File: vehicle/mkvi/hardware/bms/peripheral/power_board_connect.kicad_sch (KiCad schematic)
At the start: 1 part

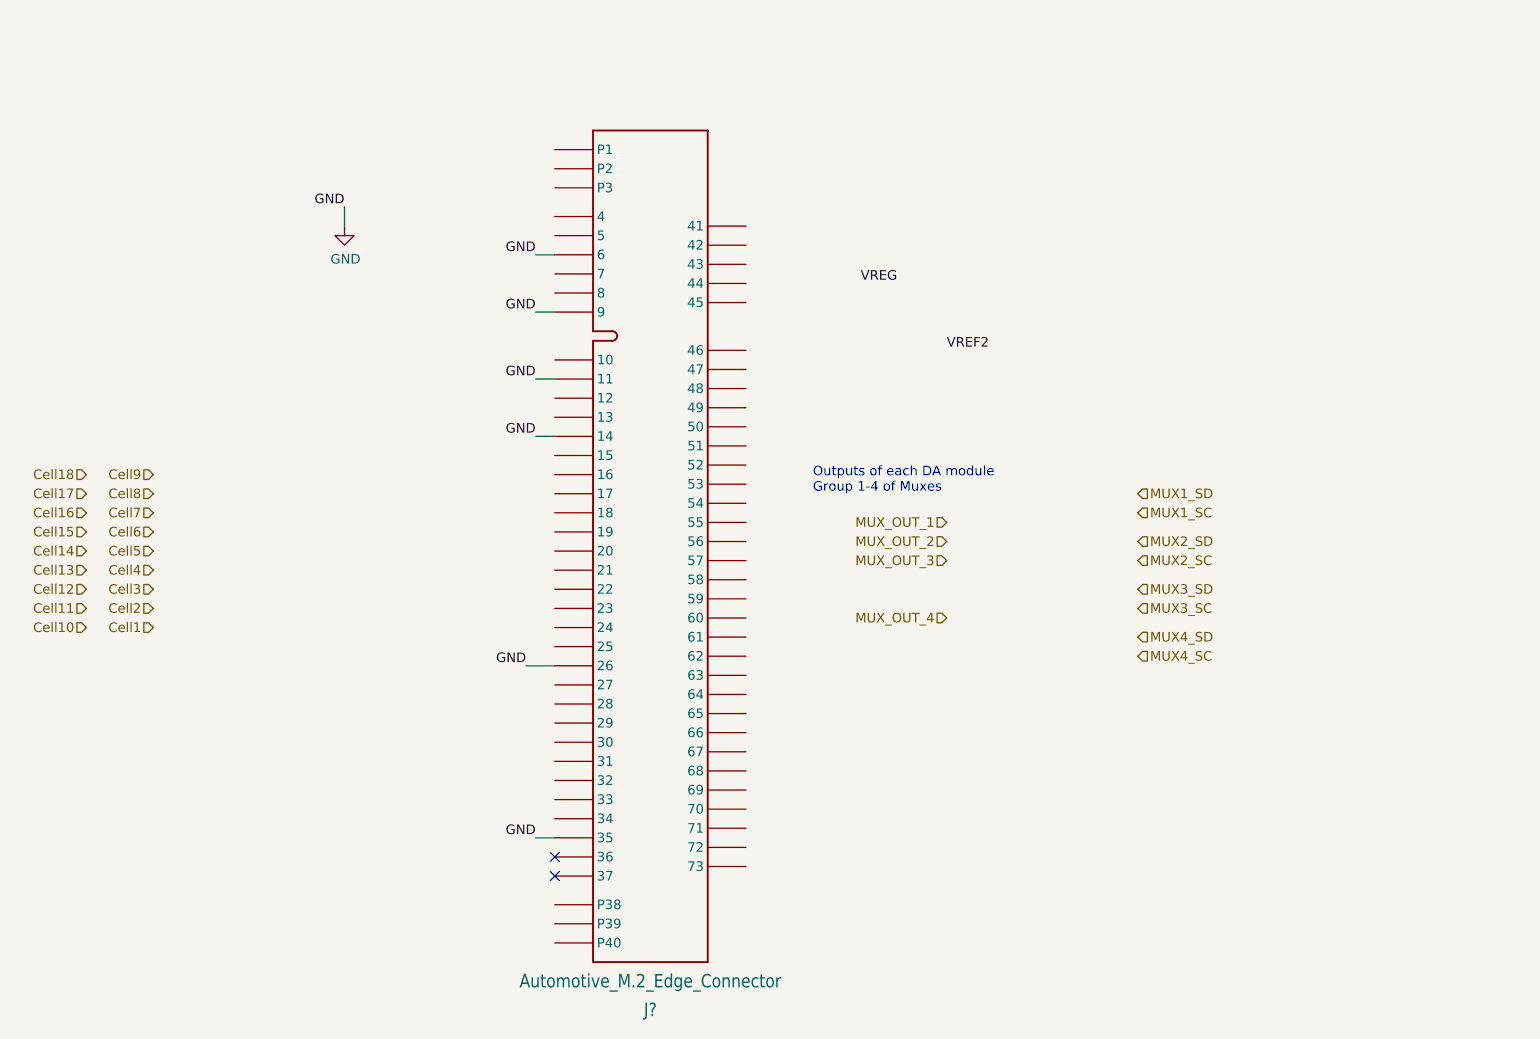
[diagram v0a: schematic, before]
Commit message: Fix transformer symbol and power flags
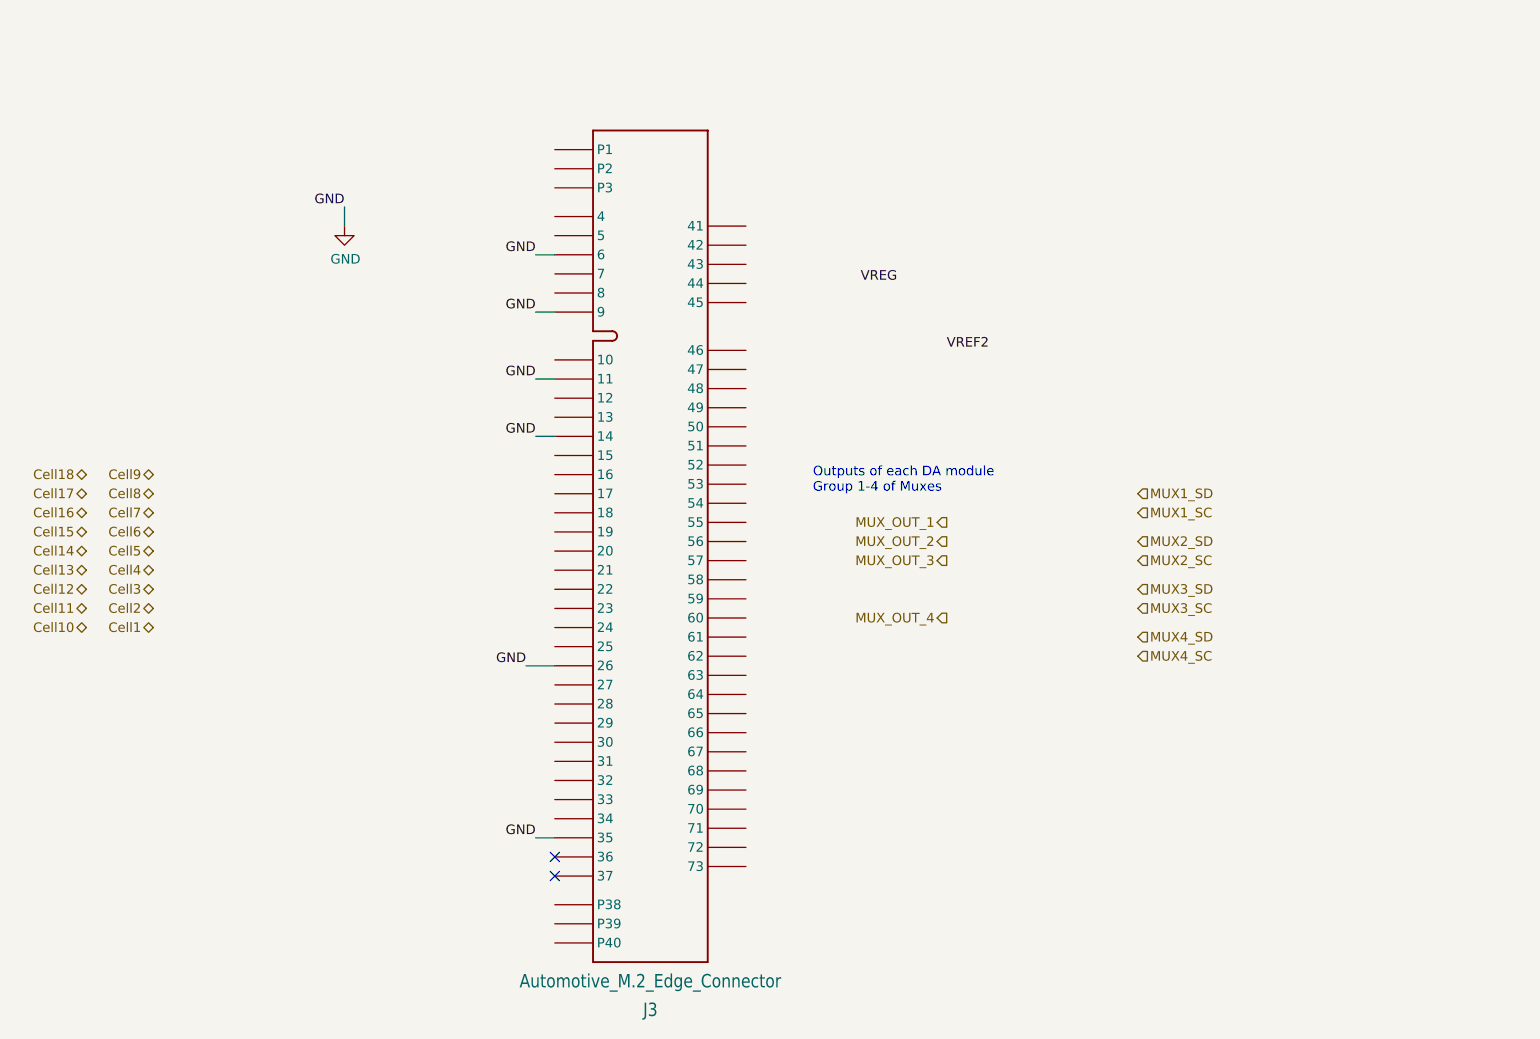
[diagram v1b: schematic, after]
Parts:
- gave numbers to parts that had none: 1
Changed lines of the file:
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@@
     (effects (font (size 1.27 1.27)) (justify right bottom))
   )
-  (hierarchical_label "MUX_OUT_4" (shape input) (at 180.34 102.87 180)
+  (hierarchical_label "MUX_OUT_4" (shape output) (at 180.34 102.87 180)
     (effects (font (size 1.27 1.27)) (justify right))
   )
-  (hierarchical_label "Cell13" (shape input) (at 66.04 96.52 180)
+  (hierarchical_label "Cell13" (shape bidirectional) (at 66.04 96.52 180)
     (effects (font (size 1.27 1.27)) (justify right))
   )
-  (hierarchical_label "Cell3" (shape input) (at 74.93 99.06 180)
+  (hierarchical_label "Cell3" (shape bidirectional) (at 74.93 99.06 180)
     (effects (font (size 1.27 1.27)) (justify right))
   )
-  (hierarchical_label "Cell1" (shape input) (at 74.93 104.14 180)
+  (hierarchical_label "Cell1" (shape bidirectional) (at 74.93 104.14 180)
     (effects (font (size 1.27 1.27)) (justify right))
   )
@@
     (effects (font (size 1.27 1.27)) (justify left))
   )
-  (hierarchical_label "Cell2" (shape input) (at 74.93 101.6 180)
+  (hierarchical_label "Cell2" (shape bidirectional) (at 74.93 101.6 180)
     (effects (font (size 1.27 1.27)) (justify right))
   )
-  (hierarchical_label "Cell12" (shape input) (at 66.04 99.06 180)
+  (hierarchical_label "Cell12" (shape bidirectional) (at 66.04 99.06 180)
     (effects (font (size 1.27 1.27)) (justify right))
   )
-  (hierarchical_label "Cell10" (shape input) (at 66.04 104.14 180)
+  (hierarchical_label "Cell10" (shape bidirectional) (at 66.04 104.14 180)
     (effects (font (size 1.27 1.27)) (justify right))
   )
@@
     (effects (font (size 1.27 1.27)) (justify left))
   )
-  (hierarchical_label "Cell11" (shape input) (at 66.04 101.6 180)
+  (hierarchical_label "Cell11" (shape bidirectional) (at 66.04 101.6 180)
     (effects (font (size 1.27 1.27)) (justify right))
   )
-  (hierarchical_label "Cell9" (shape input) (at 74.93 83.82 180)
+  (hierarchical_label "Cell9" (shape bidirectional) (at 74.93 83.82 180)
     (effects (font (size 1.27 1.27)) (justify right))
   )
-  (hierarchical_label "Cell18" (shape input) (at 66.04 83.82 180)
+  (hierarchical_label "Cell18" (shape bidirectional) (at 66.04 83.82 180)
     (effects (font (size 1.27 1.27)) (justify right))
   )
-  (hierarchical_label "MUX_OUT_3" (shape input) (at 180.34 95.25 180)
+  (hierarchical_label "MUX_OUT_3" (shape output) (at 180.34 95.25 180)
     (effects (font (size 1.27 1.27)) (justify right))
   )
-  (hierarchical_label "Cell17" (shape input) (at 66.04 86.36 180)
+  (hierarchical_label "Cell17" (shape bidirectional) (at 66.04 86.36 180)
     (effects (font (size 1.27 1.27)) (justify right))
   )
-  (hierarchical_label "MUX_OUT_2" (shape input) (at 180.34 92.71 180)
+  (hierarchical_label "MUX_OUT_2" (shape output) (at 180.34 92.71 180)
     (effects (font (size 1.27 1.27)) (justify right))
   )
-  (hierarchical_label "Cell5" (shape input) (at 74.93 93.98 180)
+  (hierarchical_label "Cell5" (shape bidirectional) (at 74.93 93.98 180)
     (effects (font (size 1.27 1.27)) (justify right))
   )
-  (hierarchical_label "Cell8" (shape input) (at 74.93 86.36 180)
+  (hierarchical_label "Cell8" (shape bidirectional) (at 74.93 86.36 180)
     (effects (font (size 1.27 1.27)) (justify right))
   )
@@
     (effects (font (size 1.27 1.27)) (justify left))
   )
-  (hierarchical_label "Cell6" (shape input) (at 74.93 91.44 180)
+  (hierarchical_label "Cell6" (shape bidirectional) (at 74.93 91.44 180)
     (effects (font (size 1.27 1.27)) (justify right))
   )
-  (hierarchical_label "MUX_OUT_1" (shape input) (at 180.34 90.17 180)
+  (hierarchical_label "MUX_OUT_1" (shape output) (at 180.34 90.17 180)
     (effects (font (size 1.27 1.27)) (justify right))
   )
@@
     (effects (font (size 1.27 1.27)) (justify left))
   )
-  (hierarchical_label "Cell16" (shape input) (at 66.04 88.9 180)
+  (hierarchical_label "Cell16" (shape bidirectional) (at 66.04 88.9 180)
     (effects (font (size 1.27 1.27)) (justify right))
   )
@@
     (effects (font (size 1.27 1.27)) (justify left))
   )
-  (hierarchical_label "Cell15" (shape input) (at 66.04 91.44 180)
+  (hierarchical_label "Cell15" (shape bidirectional) (at 66.04 91.44 180)
     (effects (font (size 1.27 1.27)) (justify right))
   )
-  (hierarchical_label "Cell4" (shape input) (at 74.93 96.52 180)
+  (hierarchical_label "Cell4" (shape bidirectional) (at 74.93 96.52 180)
     (effects (font (size 1.27 1.27)) (justify right))
   )
-  (hierarchical_label "Cell7" (shape input) (at 74.93 88.9 180)
+  (hierarchical_label "Cell7" (shape bidirectional) (at 74.93 88.9 180)
     (effects (font (size 1.27 1.27)) (justify right))
   )
-  (hierarchical_label "Cell14" (shape input) (at 66.04 93.98 180)
+  (hierarchical_label "Cell14" (shape bidirectional) (at 66.04 93.98 180)
     (effects (font (size 1.27 1.27)) (justify right))
   )
@@
   (symbol (lib_id "formula:Automotive_M.2_Edge_Connector") (at 140.97 81.28 0) (unit 1)
     (in_bom yes) (on_board yes) (fields_autoplaced)
-    (property "Reference" "J?" (id 0) (at 140.97 154.94 0)
+    (property "Reference" "J3" (id 0) (at 140.97 154.94 0)
       (effects (font (size 1.778 1.5113)))
     )

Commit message: M2 connects and new transformer on core
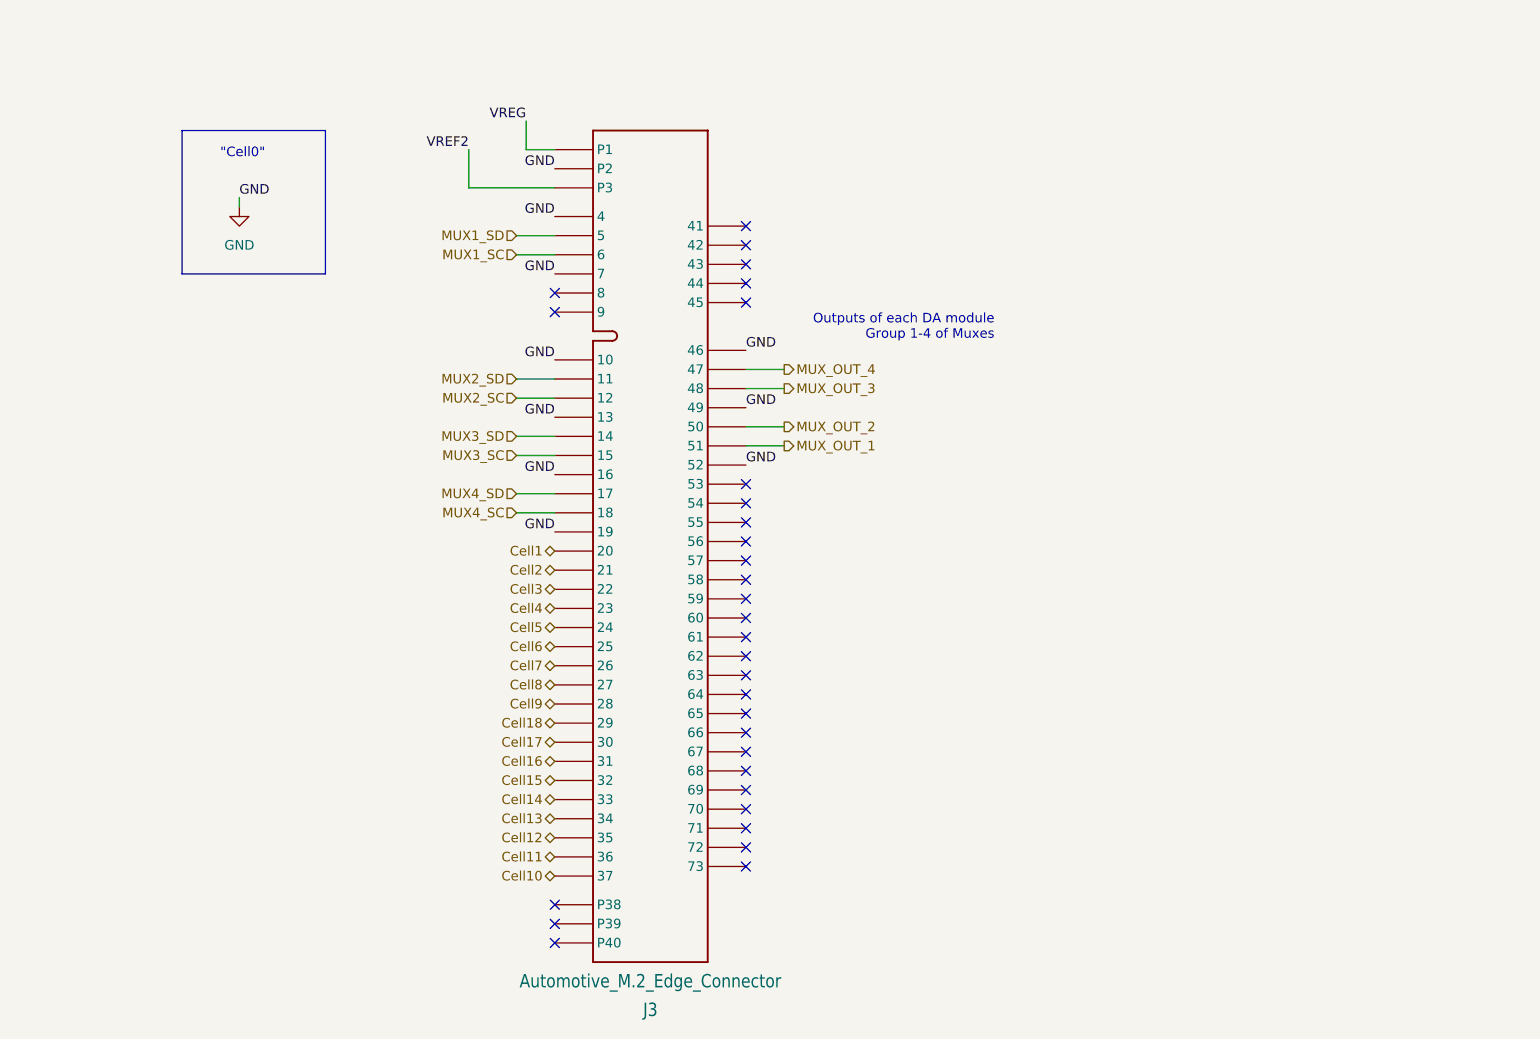
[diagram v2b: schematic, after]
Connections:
- net Cell1: now also J3.20
- net Cell10: now also J3.37
- net Cell11: now also J3.36
- net Cell12: now also J3.35
- net Cell13: now also J3.34
- net Cell14: now also J3.33
- net Cell15: now also J3.32
- net Cell16: now also J3.31
- net Cell17: now also J3.30
- net Cell18: now also J3.29
- net Cell2: now also J3.21
- net Cell3: now also J3.22
- net Cell4: now also J3.23
- net Cell5: now also J3.24
- net Cell6: now also J3.25
- net Cell7: now also J3.26
- net Cell8: now also J3.27
- net Cell9: now also J3.28
- net GND: now also J3.10, J3.13, J3.16, J3.19, J3.4, J3.46, J3.49, J3.52, J3.7, J3.P2; no longer J3.11, J3.14, J3.26, J3.35, J3.6, J3.9
- net MUX1_SC: now also J3.6
- net MUX1_SD: now also J3.5
- net MUX2_SC: now also J3.12
- net MUX2_SD: now also J3.11
- net MUX3_SC: now also J3.15
- net MUX3_SD: now also J3.14
- net MUX4_SC: now also J3.18
- net MUX4_SD: now also J3.17
- net MUX_OUT_1: now also J3.51
- net MUX_OUT_2: now also J3.50
- net MUX_OUT_3: now also J3.48
- net MUX_OUT_4: now also J3.47
- net VREF2: now also J3.P3
- net VREG: now also J3.P1
- no-connect marks 2 -> 31
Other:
- note added: ""Cell0""

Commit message: Clean schematic for peripheral and DA modules
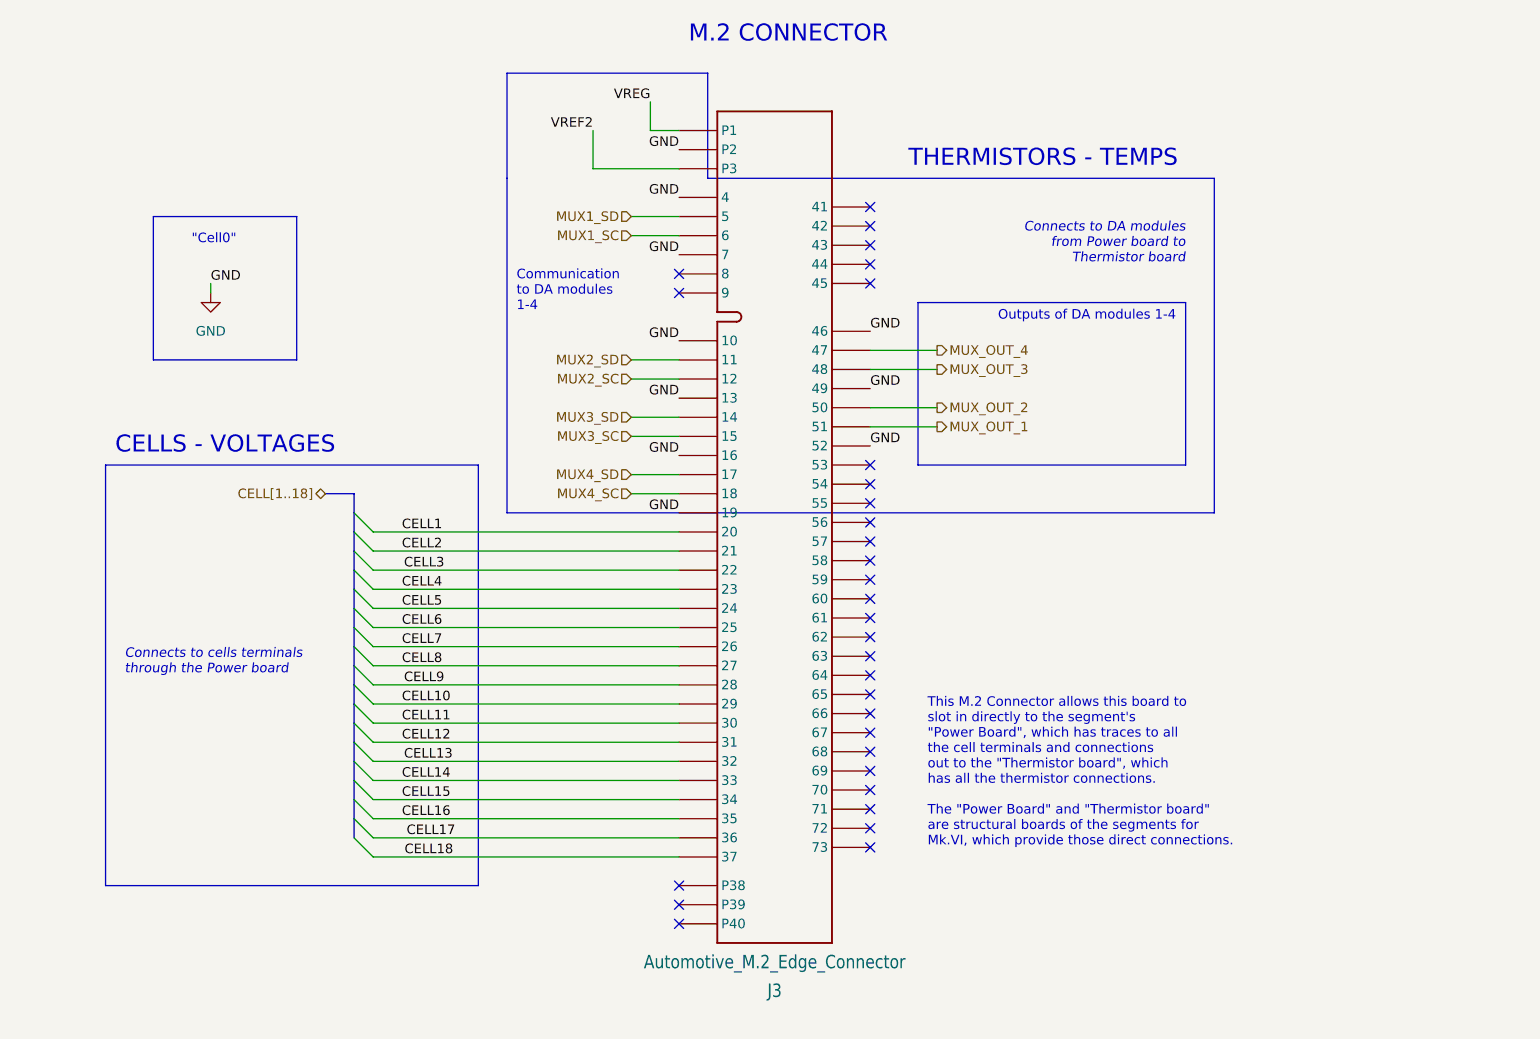
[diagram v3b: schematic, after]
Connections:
- net Cell1 renamed CELL1
- net Cell10 renamed CELL18
- net Cell11 renamed CELL17
- net Cell12 renamed CELL16
- net Cell13 renamed CELL15
- net Cell14 renamed CELL14
- net Cell15 renamed CELL13
- net Cell16 renamed CELL12
- net Cell17 renamed CELL11
- net Cell18 renamed CELL10
- net Cell2 renamed CELL2
- net Cell3 renamed CELL3
- net Cell4 renamed CELL4
- net Cell5 renamed CELL5
- net Cell6 renamed CELL6
- net Cell7 renamed CELL7
- net Cell8 renamed CELL8
- net Cell9 renamed CELL9
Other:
- note added: "CELLS - VOLTAGES"
- note added: "Communication to DA modules 1-4"
- note added: "Connects to DA modules from Power board to Thermistor board"
- note added: "Connects to cells terminals through the Power board"
- note added: "M.2 CONNECTOR"
- note added: "Outputs of DA modules 1-4"
- note added: "THERMISTORS - TEMPS"
- note added: "This M.2 Connector allows this board to slot in directly to the segment's "Power Board", which has traces to all the cell terminals and connections out to the "Thermistor board", which has all the thermistor connections. The "Power Board" and "Thermistor board" are structural boards of the segments for Mk.VI, which provide those direct connections."
- note removed: "Outputs of each DA module Group 1-4 of Muxes"
- company: (none) -> Olin Electric Motorsports
- title: (none) -> Peripheral | Power Board M.2 Connector
- moved on the sheet: J3
